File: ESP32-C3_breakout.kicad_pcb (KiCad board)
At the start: 2 copper layers, 45.7 x 21.3 mm, 31 parts, among them IC1 STF202-22T1G, J1 USB4105-GF-A, J2 Conn_01x11_Male, J3 Conn_01x11_Male, SW1 SW_Push, SW2 SW_Push, U1 LD1117S33TR_SOT223, U2 ESP32-C3, Y1 40MHz

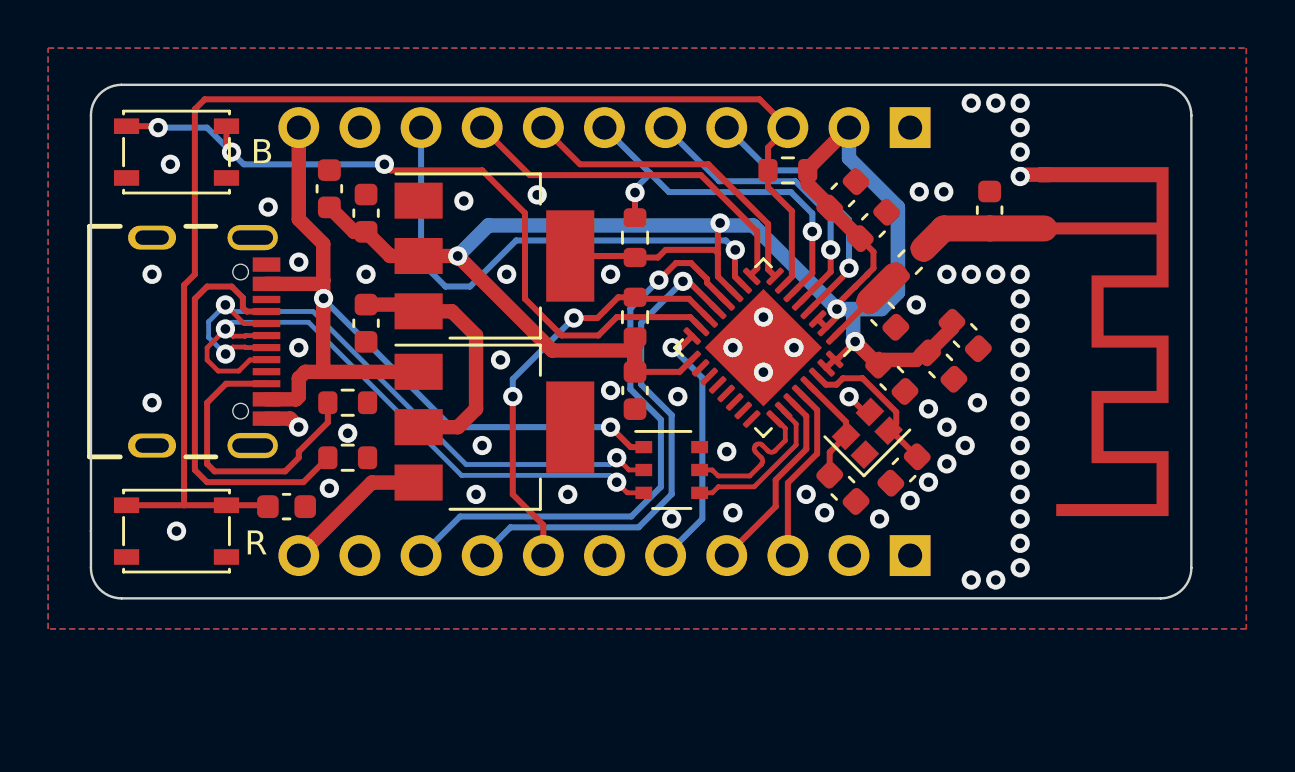
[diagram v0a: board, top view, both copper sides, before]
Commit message: Power plane improvement
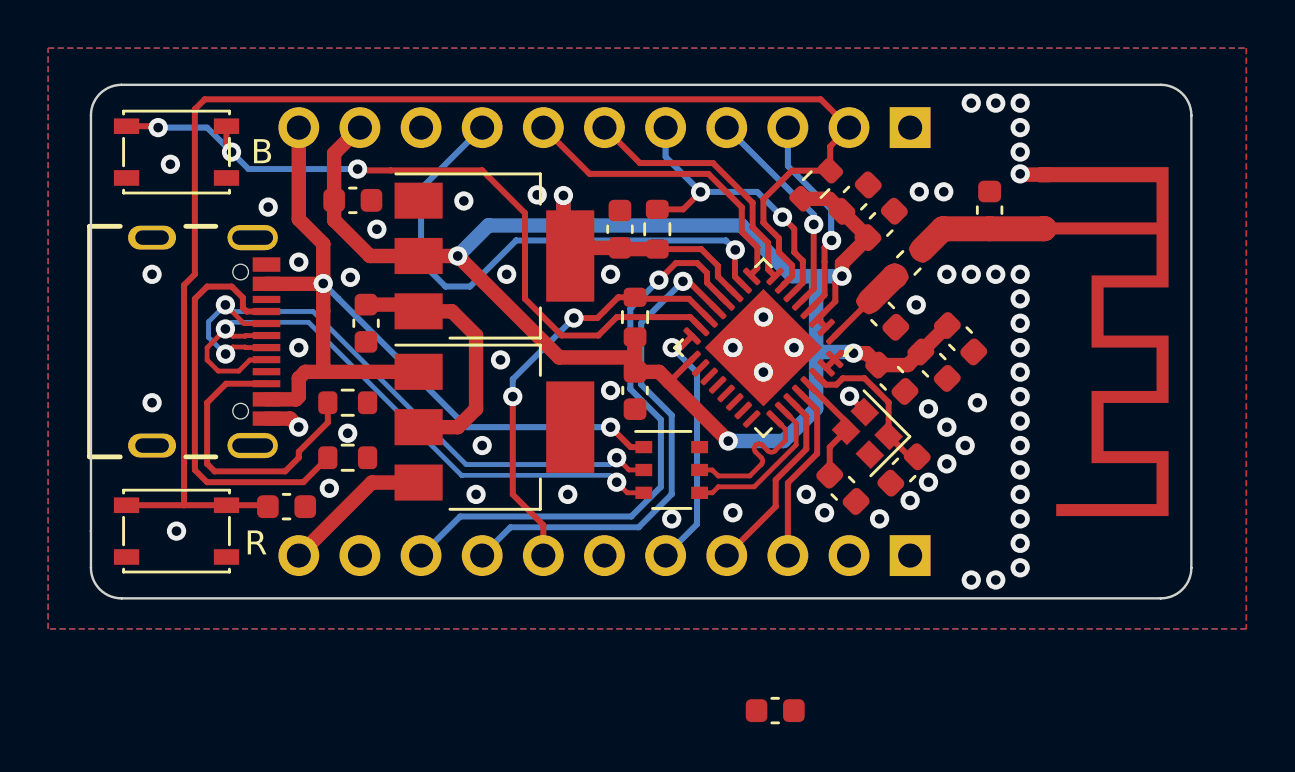
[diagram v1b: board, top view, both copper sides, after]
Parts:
- added C5: 100n, Capacitor_SMD:C_0603_1608Metric, F.Cu at (178.8, 87.2)
- C1: value 10u -> 100n
- C10: renamed from C9; value 0.1u -> 100n
- C6: renamed from C5; value 0.1u -> 100n
- moved C3 12.2 mm to (172.3, 67.2)
- moved R1 1.32 mm to (180.5, 65.4), turned to 45 degrees
- moved R4 0.99 mm to (173.9, 67.2)
- moved C2 0.77 mm to (161.2, 66.0), turned to 0 degrees
- moved C9 0.52 mm to (182.1, 65.9)
- moved C8 0.32 mm to (183.2, 67.0)
- moved C7 0.28 mm to (185.4, 72.9)
- moved C10 0.24 mm to (186.5, 71.8)
- moved L1 0.07 mm to (184.3, 68.6)
- turned Y1 to 135 degrees
- renumbered AE2 to AE1, C10 to C11, C11 to C12, C12 to C13, C13 to C14, C14 to C15, C6 to C7, C7 to C8, C8 to C9
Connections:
- C14 pad 1: Net-(C13-Pad1) -> Net-(C14-Pad1)
- C15 pad 1: Net-(C14-Pad1) -> Net-(C15-Pad1)
- J3 pad 10: GND -> +3V3
- J3 pad 2: +3V3 -> /EN
- J3 pad 3: /EN -> /GPIO0
- J3 pad 4: /GPIO0 -> /GPIO1
- J3 pad 5: /GPIO1 -> /GPIO2
- J3 pad 6: /GPIO2 -> /GPIO3
- J3 pad 7: /GPIO3 -> /GPIO4
- J3 pad 8: /GPIO4 -> /GPIO5
- J3 pad 9: /GPIO5 -> GND
- U2 pad 29: Net-(C13-Pad1) -> Net-(C14-Pad1)
- U2 pad 30: Net-(C14-Pad1) -> Net-(C15-Pad1)
- Y1 pad 1: GND -> Net-(C15-Pad1)
- Y1 pad 2: Net-(C14-Pad1) -> GND
- Y1 pad 3: GND -> Net-(C14-Pad1)
- Y1 pad 4: Net-(C13-Pad1) -> GND
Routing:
- net Net-(C15-Pad1): track 0.00 -> 6.56 mm
- net /EN: track 55.5 -> 60.2 mm
- net Net-(C13-Pad1): track 4.66 -> 0.00 mm
- net +3V3: track 77.3 -> 81.9 mm, vias 4 -> 5
- net /GPIO1: track 12.5 -> 8.97 mm
- net /GPIO2: track 15.9 -> 13.1 mm
- net /GPIO3: track 13.3 -> 10.9 mm
- net /GPIO4: track 15.2 -> 12.9 mm
- net /GPIO0: track 11.1 -> 9.22 mm
- net Net-(C14-Pad1): track 6.54 -> 4.66 mm
- net /GPIO5: track 21.6 -> 22.7 mm
- net GND: vias 66 -> 65

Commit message: General improvements
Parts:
- moved C5 11.8 mm to (170.5, 78.8), turned to 180 degrees
- moved R1 1.32 mm to (179.2, 65.2), turned to 180 degrees
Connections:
- C5 pad 1: VDD -> /USB_+5V
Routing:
- net /USB_+5V: track 36.9 -> 40.7 mm
- net /EN: track 60.2 -> 58.4 mm
- net +3V3: track 81.9 -> 80.9 mm
- net GND: track 3.65 -> 3.47 mm, vias 65 -> 73
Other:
- board text added: "VIN"
- board text removed: "5V IN"

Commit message: Version 2
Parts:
- removed C5: 100n, Capacitor_SMD:C_0603_1608Metric
- added R6: 10k, Resistor_SMD:R_0603_1608Metric, F.Cu at (161.3, 72.7)
- U1: footprint Package_TO_SOT_SMD:SOT-223-3_TabPin2 -> Package_TO_SOT_SMD:SOT-89-3
- moved C4 31.5 mm to (186.2, 63.8), turned to -90 degrees
- moved C2 13.3 mm to (174.4, 67.2), turned to 90 degrees
- moved C3 3.20 mm to (169.1, 67.2)
- moved R5 2.61 mm to (171.2, 68.9), turned to -90 degrees
- moved U1 2.34 mm to (164.8, 67.8)
- moved R3 1.90 mm to (159.7, 75.8), turned to 90 degrees
- moved IC1 1.59 mm to (173.3, 76.1)
- moved C1 1.57 mm to (161.3, 69.6)
- moved D1 1.37 mm to (166.6, 74.2)
- moved C11 1.22 mm to (172.7, 72.7)
- moved R4 1.05 mm to (172.8, 67.2)
- moved R2 0.95 mm to (161.3, 75.8), turned to 90 degrees
- moved SW1 0.72 mm to (154.6, 79.8)
- moved SW2 0.72 mm to (154.6, 64.0)
- moved R1 0.64 mm to (179.1, 65.8)
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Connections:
- D1 pad 2: VDD -> (no net)
- D1 pad 4: (no net) -> VDD
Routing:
- net +3V3: track 80.9 -> 88.8 mm, vias 5 -> 6
- net /GPIO2: track 13.1 -> 19.0 mm, vias 2 -> 3
- net /USB_+5V: track 40.7 -> 36.3 mm
- net /EN: track 58.4 -> 62.4 mm
- net /GPIO8: track 17.8 -> 21.5 mm
- net /BOOT: track 31.2 -> 27.9 mm
- net VDD: track 10.9 -> 13.6 mm
- net Net-(J1-PadB5): track 12.3 -> 10.3 mm
- net /GPIO7: track 20.5 -> 18.9 mm
- net /GPIO6: track 24.3 -> 22.8 mm
- net GND: track 3.47 -> 1.99 mm, vias 73 -> 68
- net /D_N: track 26.9 -> 25.6 mm
- net Net-(J1-PadA5): track 17.1 -> 18.3 mm
- net /D_P: track 26.7 -> 25.7 mm
- net /VIN: track 6.23 -> 7.07 mm
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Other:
- board text added: "0"
- board text added: "1"
- board text added: "10"
- board text added: "2"
- board text added: "3"
- board text added: "4"
- board text added: "5"
- board text added: "5V USB"
- board text added: "6"
- board text added: "7"
- board text added: "8"
- board text added: "9"
- board text added: "E"
- board text added: "G"
